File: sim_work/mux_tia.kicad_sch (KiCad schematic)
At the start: 6 parts, among them U1 ADA4530-1

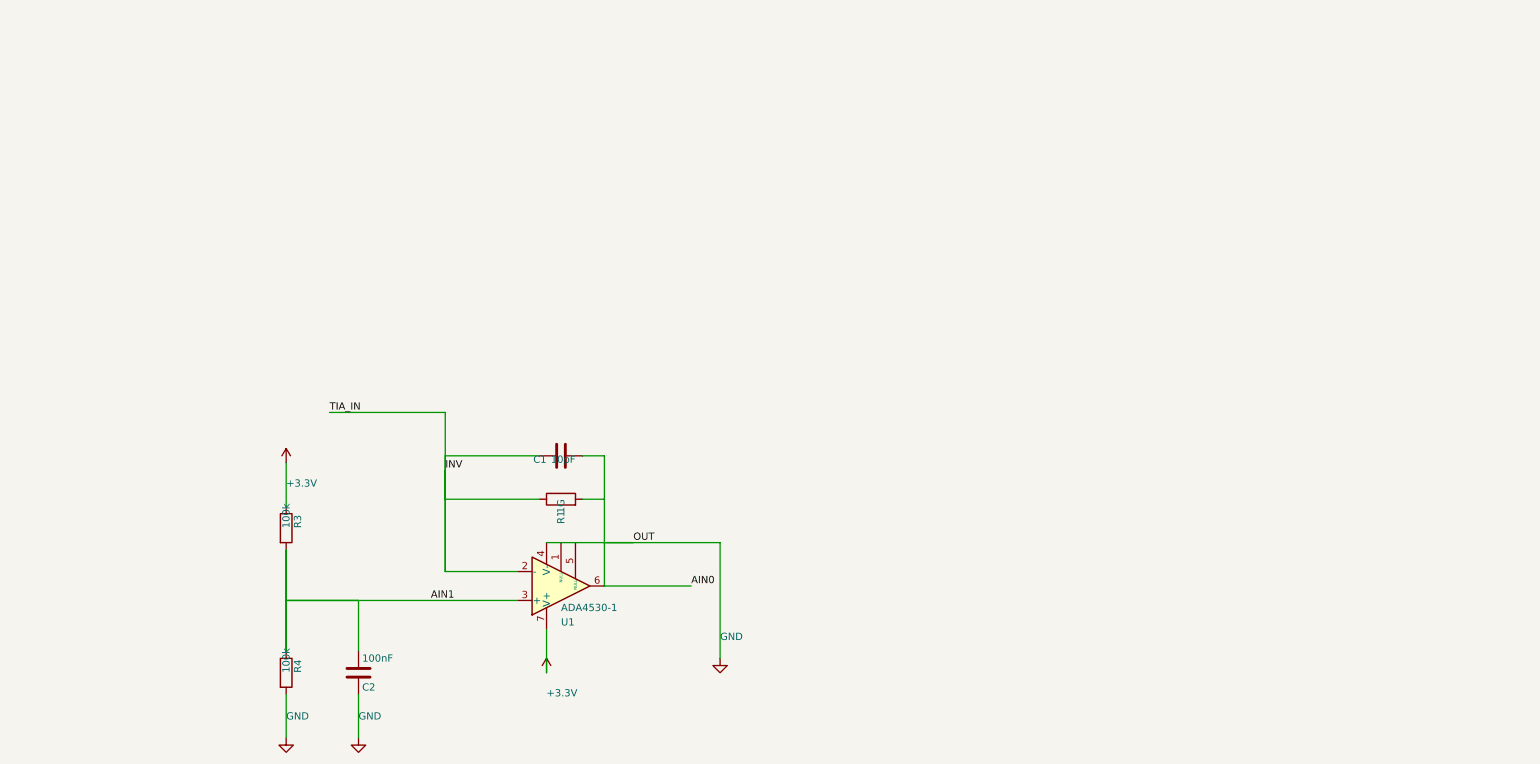
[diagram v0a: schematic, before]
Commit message: Fix schematic connections, add docs and repo portability
- Input filters: R rotation=90 (horizontal), ESD diode rotations fixed,
  junction dots at cathode-signal connection, wires to GND symbols
- Relay ladder: flyback diode rotation 270->90 (K top, A bottom)
- Electrometer/Mux TIA: 4 junction dots each at T-junctions
- AD636 RMS detector: proper IC box with pin labels replaces text-only
- Oscillator blocks: D_Zener symbol, L-shaped cathode routing
- TIA blocks: title/function annotations on all 5 blocks
- New: requirements.txt, docs/oscillator_guide.md
- D_Zener.kicad_sym added to bundled symbols/
- .gitignore updated for docs/ and requirements.txt
- README updated with pip install -r requirements.txt
- PROJECT.md session 9 changelog
- SimGUI builds clean (0 errors)

Co-Authored-By: Claude Opus 4.6 <noreply@anthropic.com>
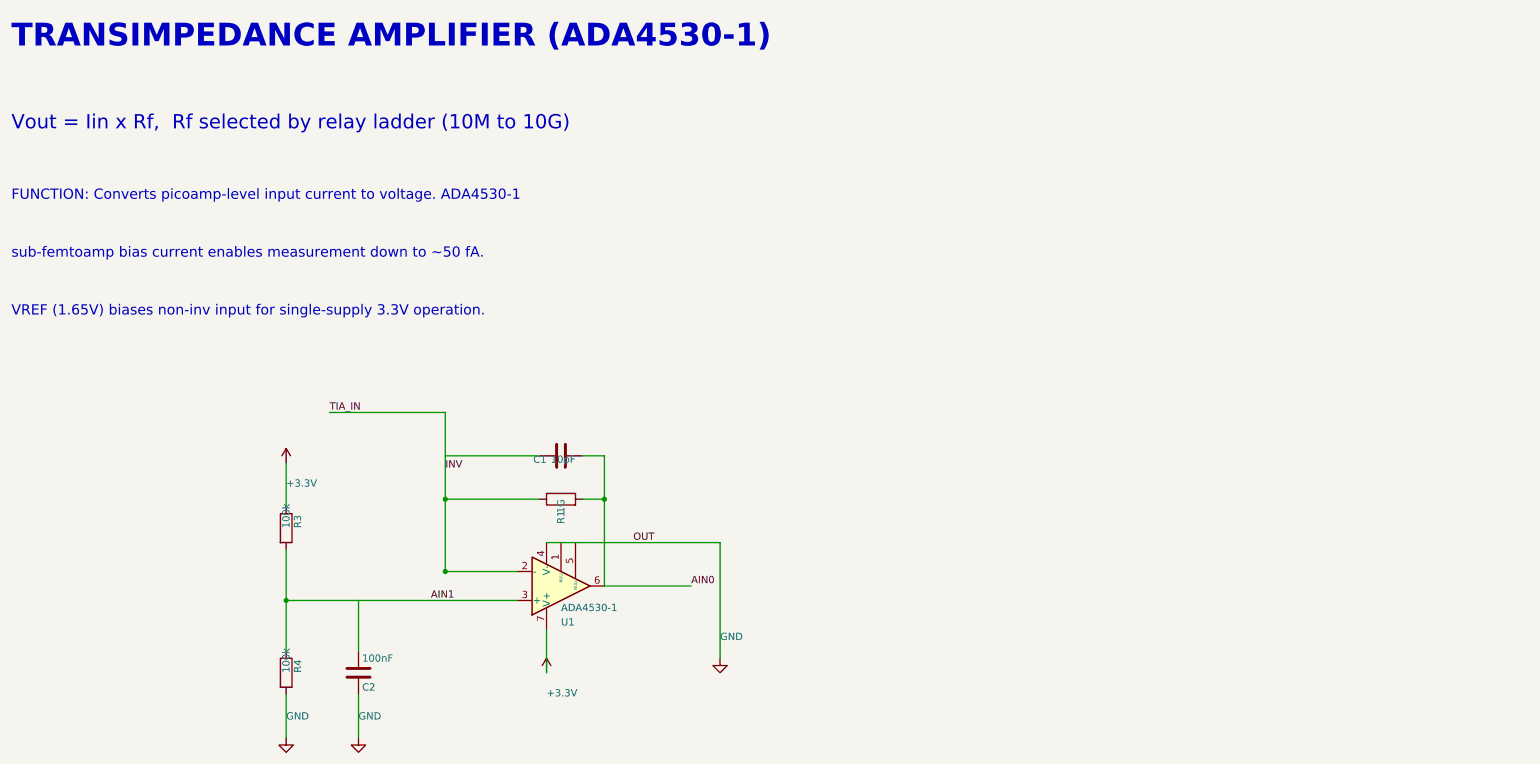
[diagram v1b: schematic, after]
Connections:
- net AIN1: no longer C2.1
- net INV: no longer C1.1
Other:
- note added: "FUNCTION: Converts picoamp-level input current to voltage. ADA4530-1"
- note added: "TRANSIMPEDANCE AMPLIFIER (ADA4530-1)"
- note added: "VREF (1.65V) biases non-inv input for single-supply 3.3V operation."
- note added: "Vout = Iin x Rf, Rf selected by relay ladder (10M to 10G)"
- note added: "sub-femtoamp bias current enables measurement down to ~50 fA."
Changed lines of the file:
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@@
 		(instances
 			(project "TIA with Mux Interface - ADA4530-1"
-				(path "/5a34846a-3a73-4a4a-af9b-cc667487aea5"
+				(path "/053c9402-6d6b-4cfa-a10d-6d29029a580d"
 					(reference "U1")
 					(unit 1)
@@
 		(instances
 			(project "TIA with Mux Interface - ADA4530-1"
-				(path "/5a34846a-3a73-4a4a-af9b-cc667487aea5"
+				(path "/053c9402-6d6b-4cfa-a10d-6d29029a580d"
 					(reference "R1")
 					(unit 1)
@@
 		(instances
 			(project "TIA with Mux Interface - ADA4530-1"
-				(path "/5a34846a-3a73-4a4a-af9b-cc667487aea5"
+				(path "/053c9402-6d6b-4cfa-a10d-6d29029a580d"
 					(reference "C1")
 					(unit 1)
@@
 		(instances
 			(project "TIA with Mux Interface - ADA4530-1"
-				(path "/5a34846a-3a73-4a4a-af9b-cc667487aea5"
+				(path "/053c9402-6d6b-4cfa-a10d-6d29029a580d"
 					(reference "R3")
 					(unit 1)
@@
 		(instances
 			(project "TIA with Mux Interface - ADA4530-1"
-				(path "/5a34846a-3a73-4a4a-af9b-cc667487aea5"
+				(path "/053c9402-6d6b-4cfa-a10d-6d29029a580d"
 					(reference "R4")
 					(unit 1)
@@
 		(instances
 			(project "TIA with Mux Interface - ADA4530-1"
-				(path "/5a34846a-3a73-4a4a-af9b-cc667487aea5"
+				(path "/053c9402-6d6b-4cfa-a10d-6d29029a580d"
 					(reference "C2")
 					(unit 1)
@@
 		(instances
 			(project "TIA with Mux Interface - ADA4530-1"
-				(path "/5a34846a-3a73-4a4a-af9b-cc667487aea5"
+				(path "/053c9402-6d6b-4cfa-a10d-6d29029a580d"
 					(reference "#PWR01")
 					(unit 1)
@@
 		(instances
 			(project "TIA with Mux Interface - ADA4530-1"
-				(path "/5a34846a-3a73-4a4a-af9b-cc667487aea5"
+				(path "/053c9402-6d6b-4cfa-a10d-6d29029a580d"
 					(reference "#PWR02")
 					(unit 1)
@@
 		(instances
 			(project "TIA with Mux Interface - ADA4530-1"
-				(path "/5a34846a-3a73-4a4a-af9b-cc667487aea5"
+				(path "/053c9402-6d6b-4cfa-a10d-6d29029a580d"
 					(reference "#PWR03")
 					(unit 1)
@@
 		(instances
 			(project "TIA with Mux Interface - ADA4530-1"
-				(path "/5a34846a-3a73-4a4a-af9b-cc667487aea5"
+				(path "/053c9402-6d6b-4cfa-a10d-6d29029a580d"
 					(reference "#PWR04")
 					(unit 1)
@@
 		(instances
 			(project "TIA with Mux Interface - ADA4530-1"
-				(path "/5a34846a-3a73-4a4a-af9b-cc667487aea5"
+				(path "/053c9402-6d6b-4cfa-a10d-6d29029a580d"
 					(reference "#PWR05")
 					(unit 1)
@@
 	(wire
 		(pts
-			(xy 96.52 109.22) (xy 96.52 96.52)
-		)
-		(stroke
-			(width 0)
-			(type default)
-		)
-	)
-	(wire
-		(pts
 			(xy 96.52 96.52) (xy 113.03 96.52)
 		)
@@
 	(wire
 		(pts
-			(xy 96.52 96.52) (xy 96.52 88.9)
-		)
-		(stroke
-			(width 0)
-			(type default)
-		)
-	)
-	(wire
-		(pts
 			(xy 96.52 88.9) (xy 113.03 88.9)
 		)
@@
 	(wire
 		(pts
-			(xy 96.52 91.44) (xy 96.52 96.52)
-		)
-		(stroke
-			(width 0)
-			(type default)
-		)
-	)
-	(wire
-		(pts
-			(xy 124.46 104.14) (xy 129.54 104.14)
-		)
-		(stroke
-			(width 0)
-			(type default)
-		)
-	)
-	(wire
-		(pts
 			(xy 68.58 105.41) (xy 68.58 123.19)
 		)
@@
 	(wire
 		(pts
-			(xy 68.58 105.41) (xy 68.58 114.3)
-		)
-		(stroke
-			(width 0)
-			(type default)
-		)
-	)
-	(wire
-		(pts
-			(xy 68.58 114.3) (xy 68.58 123.19)
+			(xy 81.28 114.3) (xy 81.28 123.19)
 		)
 		(stroke
@@
 	(wire
 		(pts
-			(xy 81.28 123.19) (xy 81.28 114.3)
-		)
-		(stroke
-			(width 0)
-			(type default)
-		)
-	)
-	(wire
-		(pts
-			(xy 81.28 114.3) (xy 68.58 114.3)
-		)
-		(stroke
-			(width 0)
-			(type default)
-		)
-	)
-	(wire
-		(pts
 			(xy 124.46 111.76) (xy 139.7 111.76)
 		)
@@
 	(wire
 		(pts
-			(xy 68.58 97.79) (xy 68.58 90.17)
+			(xy 68.58 90.17) (xy 68.58 97.79)
 		)
 		(stroke
@@
 			(type default)
 		)
+	)
+	(junction
+		(at 96.52 109.22)
+		(diameter 0)
+		(color 0 0 0 0)
+	)
+	(junction
+		(at 96.52 96.52)
+		(diameter 0)
+		(color 0 0 0 0)
+	)
+	(junction
+		(at 124.46 96.52)
+		(diameter 0)
+		(color 0 0 0 0)
+	)
+	(junction
+		(at 68.58 114.3)
+		(diameter 0)
+		(color 0 0 0 0)
 	)
 	(label "TIA_IN"
@@
 		)
 	)
+	(text "TRANSIMPEDANCE AMPLIFIER (ADA4530-1)"
+		(exclude_from_sim no)
+		(at 20.32 15.24 0.0000)
+		(effects
+			(font
+				(size 4 4)
+				(bold yes)
+			)
+			(justify left)
+		)
+	)
+	(text "Vout = Iin x Rf,  Rf selected by relay ladder (10M to 10G)"
+		(exclude_from_sim no)
+		(at 20.32 30.48 0.0000)
+		(effects
+			(font
+				(size 2.5 2.5)
+			)
+			(justify left)
+		)
+	)
+	(text "FUNCTION: Converts picoamp-level input current to voltage. ADA4530-1"
+		(exclude_from_sim no)
+		(at 20.32 43.18 0.0000)
+		(effects
+			(font
+				(size 1.8 1.8)
+			)
+			(justify left)
+		)
+	)
+	(text "sub-femtoamp bias current enables measurement down to ~50 fA."
+		(exclude_from_sim no)
+		(at 20.32 53.34 0.0000)
+		(effects
+			(font
+				(size 1.8 1.8)
+			)
+			(justify left)
+		)
+	)
+	(text "VREF (1.65V) biases non-inv input for single-supply 3.3V operation."
+		(exclude_from_sim no)
+		(at 20.32 63.5 0.0000)
+		(effects
+			(font
+				(size 1.8 1.8)
+			)
+			(justify left)
+		)
+	)

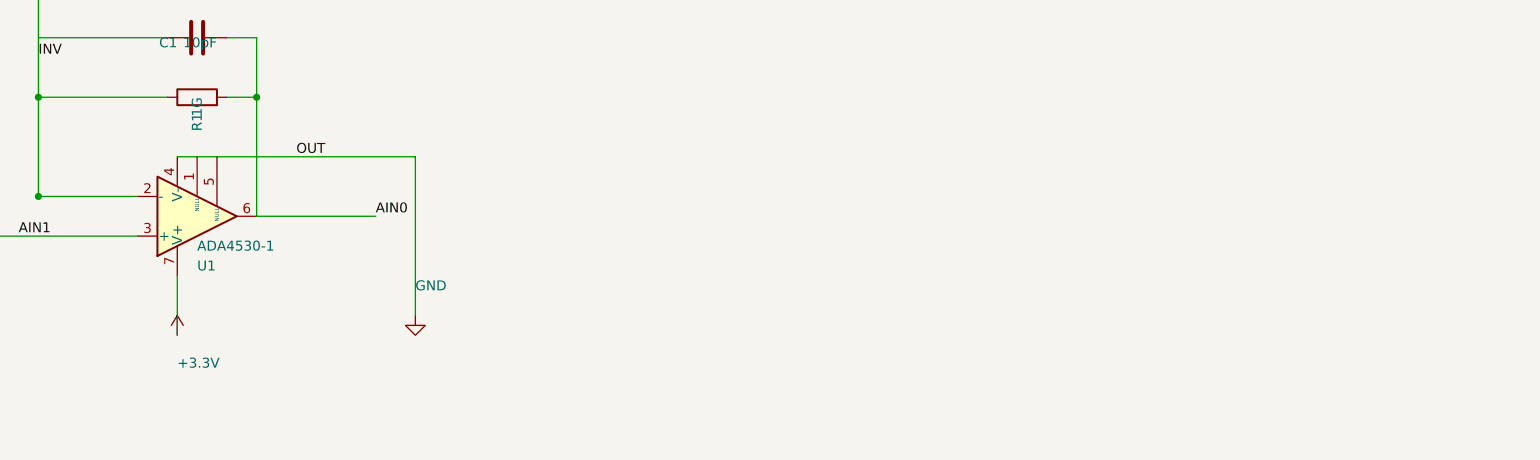
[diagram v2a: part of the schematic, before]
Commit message: Add comparison mode, fix SimGUI subprocess popups, DAC7800 IC boxes
- SimGUI: fix Python path detection (FindPython searches Python312/313/311)
- SimGUI: suppress console popup windows (CREATE_NO_WINDOW for subprocess)
- SimGUI: add Comparison project (MDAC vs Analog oscillator side-by-side)
- SimGUI: fix async wrapping (direct await instead of Task.Run)
- Pipeline: draw DAC7800 as proper IC box with pin labels (VREF/IOUT/VCTRL)
- Pipeline: fix electrometer_362 layout (spacing, junction dots at T-junctions)
- Pipeline: fix summing amp gain annotations (BP=-0.455, not -2.2)
- Pipeline: add analog_osc command for friend's SVF oscillator simulation
- Docs: comparison_guide.md, updated README and PROJECT tracker

Co-Authored-By: Claude Opus 4.6 <noreply@anthropic.com>
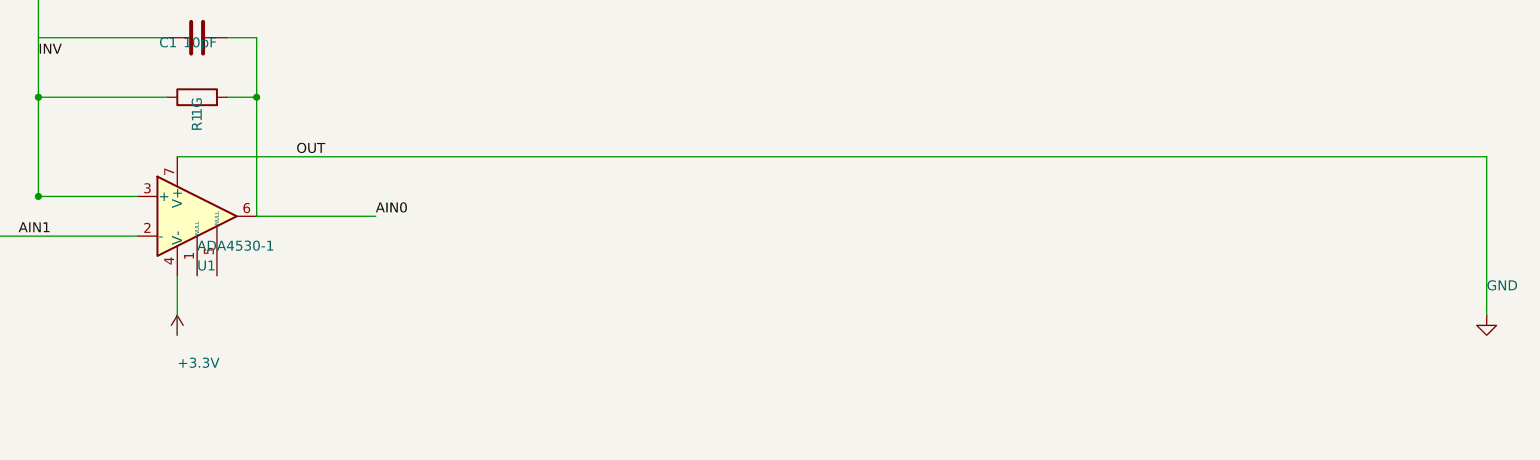
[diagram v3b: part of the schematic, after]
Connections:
- net +3.3V: now also U1.4 (V-); no longer U1.7 (V+)
- net AIN1: now also U1.2 (-); no longer U1.3 (+)
- net GND: now also U1.7 (V+); no longer U1.4 (V-)
- net INV: now also U1.3 (+); no longer U1.2 (-)
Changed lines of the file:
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@@
 		(lib_id "LM741:LM741")
 		(at 116.84 111.76 0)
-		(mirror x)
 		(unit 1)
 		(exclude_from_sim no)
@@
 		(instances
 			(project "TIA with Mux Interface - ADA4530-1"
-				(path "/602dabe6-c8b9-4c4d-a472-bf9b5063692f"
+				(path "/e9fb5415-4ca6-4d3c-a70a-bf2254619839"
 					(reference "U1")
 					(unit 1)
@@
 		(instances
 			(project "TIA with Mux Interface - ADA4530-1"
-				(path "/602dabe6-c8b9-4c4d-a472-bf9b5063692f"
+				(path "/e9fb5415-4ca6-4d3c-a70a-bf2254619839"
 					(reference "R1")
 					(unit 1)
@@
 		(instances
 			(project "TIA with Mux Interface - ADA4530-1"
-				(path "/602dabe6-c8b9-4c4d-a472-bf9b5063692f"
+				(path "/e9fb5415-4ca6-4d3c-a70a-bf2254619839"
 					(reference "C1")
 					(unit 1)
@@
 		(instances
 			(project "TIA with Mux Interface - ADA4530-1"
-				(path "/602dabe6-c8b9-4c4d-a472-bf9b5063692f"
+				(path "/e9fb5415-4ca6-4d3c-a70a-bf2254619839"
 					(reference "R3")
 					(unit 1)
@@
 		(instances
 			(project "TIA with Mux Interface - ADA4530-1"
-				(path "/602dabe6-c8b9-4c4d-a472-bf9b5063692f"
+				(path "/e9fb5415-4ca6-4d3c-a70a-bf2254619839"
 					(reference "R4")
 					(unit 1)
@@
 		(instances
 			(project "TIA with Mux Interface - ADA4530-1"
-				(path "/602dabe6-c8b9-4c4d-a472-bf9b5063692f"
+				(path "/e9fb5415-4ca6-4d3c-a70a-bf2254619839"
 					(reference "C2")
 					(unit 1)
@@
 		(instances
 			(project "TIA with Mux Interface - ADA4530-1"
-				(path "/602dabe6-c8b9-4c4d-a472-bf9b5063692f"
+				(path "/e9fb5415-4ca6-4d3c-a70a-bf2254619839"
 					(reference "#PWR01")
 					(unit 1)
@@
 	(symbol
 		(lib_id "GND:GND")
-		(at 144.78 124.46 0)
+		(at 281.94 124.46 0)
 		(unit 1)
 		(exclude_from_sim no)
@@
 		(fields_autoplaced no)
 		(property "Reference" "#PWR02"
-			(at 144.78 118.11 0.0000)
+			(at 281.94 118.11 0.0000)
 			(hide yes)
 			(effects
@@
 		)
 		(property "Value" "GND"
-			(at 144.78 120.65 0.0000)
-			(effects
-				(font
-					(size 1.27 1.27)
-				)
-				(justify left)
-			)
-		)
-		(pin "1"
-		)
-		(instances
-			(project "TIA with Mux Interface - ADA4530-1"
-				(path "/602dabe6-c8b9-4c4d-a472-bf9b5063692f"
+			(at 281.94 120.65 0.0000)
+			(effects
+				(font
+					(size 1.27 1.27)
+				)
+				(justify left)
+			)
+		)
+		(pin "1"
+		)
+		(instances
+			(project "TIA with Mux Interface - ADA4530-1"
+				(path "/e9fb5415-4ca6-4d3c-a70a-bf2254619839"
 					(reference "#PWR02")
 					(unit 1)
@@
 		(instances
 			(project "TIA with Mux Interface - ADA4530-1"
-				(path "/602dabe6-c8b9-4c4d-a472-bf9b5063692f"
+				(path "/e9fb5415-4ca6-4d3c-a70a-bf2254619839"
 					(reference "#PWR03")
 					(unit 1)
@@
 		(instances
 			(project "TIA with Mux Interface - ADA4530-1"
-				(path "/602dabe6-c8b9-4c4d-a472-bf9b5063692f"
+				(path "/e9fb5415-4ca6-4d3c-a70a-bf2254619839"
 					(reference "#PWR04")
 					(unit 1)
@@
 		(instances
 			(project "TIA with Mux Interface - ADA4530-1"
-				(path "/602dabe6-c8b9-4c4d-a472-bf9b5063692f"
+				(path "/e9fb5415-4ca6-4d3c-a70a-bf2254619839"
 					(reference "#PWR05")
 					(unit 1)
@@
 	(wire
 		(pts
-			(xy 114.3 104.14) (xy 144.78 104.14)
-		)
-		(stroke
-			(width 0)
-			(type default)
-		)
-	)
-	(wire
-		(pts
-			(xy 144.78 104.14) (xy 144.78 124.46)
-		)
-		(stroke
+			(xy 114.3 104.14) (xy 281.94 104.14)
+		)
+		(stroke
+			(width 0)
+			(type default)
+		)
+	)
+	(wire
+		(pts
+			(xy 281.94 104.14) (xy 281.94 124.46)
+		)
+		(stroke
